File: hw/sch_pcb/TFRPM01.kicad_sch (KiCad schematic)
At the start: 28 parts, among them J1 DS1022-1*40RDF11-B, J2 SM04B-GHS-TB, J3 SM04B-GHS-TB, M2 M3, U1 PCF8583T, U2 SN74LVC1G14QDCKRQ1, U3 MIC5504-3.3YM5

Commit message: Cleanup schematics.
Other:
- moved on the sheet: J3, R10

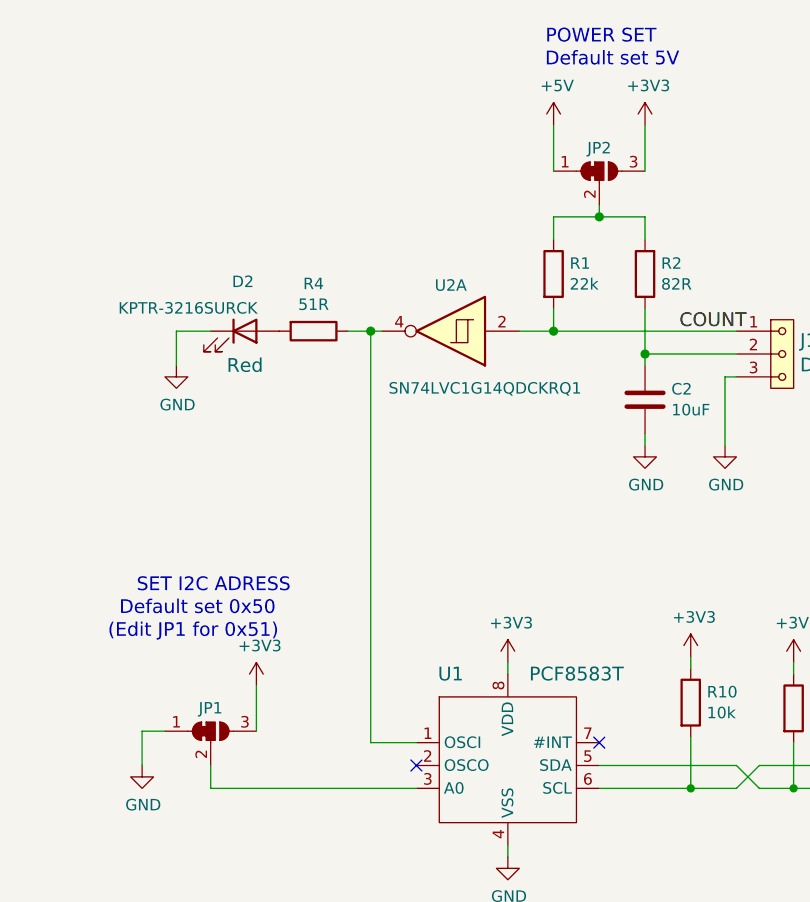
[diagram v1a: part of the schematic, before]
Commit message: Update schematics symbols and PCBs to resolve errors in action run.
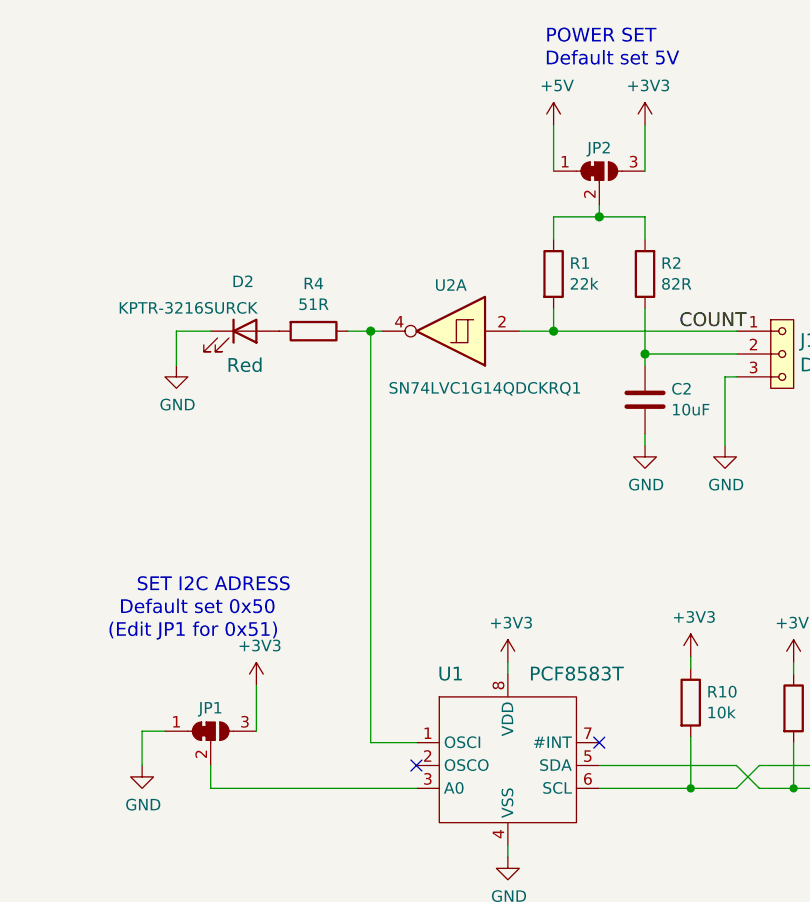
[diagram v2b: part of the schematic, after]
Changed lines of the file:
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@@
       (effects (font (size 1.524 1.524)) hide)
     )
-    (property "Datasheet" "" (at 35.56 175.26 0)
+    (property "Datasheet" "~" (at 35.56 175.26 0)
       (effects (font (size 1.524 1.524)))
     )
@@
       (effects (font (size 1.524 1.524)) hide)
     )
-    (property "Datasheet" "" (at 133.35 95.25 0)
+    (property "Datasheet" "https://www.nxp.com/docs/en/data-sheet/PCF8583.pdf" (at 133.35 95.25 0)
       (effects (font (size 1.524 1.524)) hide)
     )
@@
       (effects (font (size 1.27 1.27)) hide)
     )
-    (property "Datasheet" "" (at 165.1 105.41 0)
+    (property "Datasheet" "~" (at 165.1 105.41 0)
       (effects (font (size 1.27 1.27)) hide)
     )
@@
       (effects (font (size 1.27 1.27)) hide)
     )
-    (property "Datasheet" "" (at 153.67 104.775 0)
+    (property "Datasheet" "~" (at 153.67 104.775 0)
       (effects (font (size 1.27 1.27)) hide)
     )
@@
       (effects (font (size 1.524 1.524)) hide)
     )
-    (property "Datasheet" "" (at 27.94 175.26 0)
+    (property "Datasheet" "~" (at 27.94 175.26 0)
       (effects (font (size 1.524 1.524)))
     )
@@
     )
     (property "Datasheet" "http://www.ti.com/lit/gpn/sn74HC14" (at 127 63.5 0)
-      (effects (font (size 1.27 1.27)) hide)
-    )
-    (property "UST_id" "" (at 127 63.5 0)
       (effects (font (size 1.27 1.27)) hide)
     )
@@
     )
   )
-  (symbol (lib_name "LED_1") (lib_id "Device:LED") (at 104.14 63.5 0) (unit 1)
+  (symbol (lib_id "Device:LED") (at 104.14 63.5 0) (unit 1)
     (in_bom yes) (on_board yes) (dnp no)
     (property "Reference" "D2" (at 103.9114 58.0136 0)
@@
       (effects (font (size 1.27 1.27)) hide)
     )
-    (property "Datasheet" "https://www.tme.eu/Document/abfabb2e369b55022af776cff528b52b/kptr-3216surck.pdf" (at 104.14 63.5 0)
+    (property "Datasheet" "~" (at 104.14 63.5 0)
       (effects (font (size 1.27 1.27)) hide)
     )
@@
       (effects (font (size 1.27 1.27)) hide)
     )
-    (property "Datasheet" "" (at 138.43 57.15 0)
+    (property "Datasheet" "~" (at 138.43 57.15 0)
       (effects (font (size 1.27 1.27)) hide)
     )
@@
       (effects (font (size 1.27 1.27)) hide)
     )
-    (property "Datasheet" "" (at 111.76 63.5 0)
+    (property "Datasheet" "~" (at 111.76 63.5 0)
       (effects (font (size 1.27 1.27)) hide)
     )
@@
       (effects (font (size 1.27 1.27)) hide)
     )
-    (property "Datasheet" "" (at 148.59 71.12 0)
+    (property "Datasheet" "~" (at 148.59 71.12 0)
       (effects (font (size 1.27 1.27)) hide)
     )
@@
     )
     (property "Datasheet" "http://ww1.microchip.com/downloads/en/DeviceDoc/MIC550X.pdf" (at 60.96 165.1 0)
-      (effects (font (size 1.27 1.27)) hide)
-    )
-    (property "UST_id" "" (at 67.31 171.45 0)
       (effects (font (size 1.27 1.27)) hide)
     )
@@
       (effects (font (size 1.524 1.524)) hide)
     )
-    (property "Datasheet" "" (at 26.67 137.16 0)
+    (property "Datasheet" "~" (at 26.67 137.16 0)
       (effects (font (size 1.524 1.524)))
     )
@@
       (effects (font (size 1.524 1.524)) hide)
     )
-    (property "Datasheet" "" (at 35.56 137.16 0)
+    (property "Datasheet" "~" (at 35.56 137.16 0)
       (effects (font (size 1.524 1.524)))
     )
@@
       (effects (font (size 1.27 1.27)) hide)
     )
-    (property "Datasheet" "" (at 81.28 175.26 0)
+    (property "Datasheet" "~" (at 81.28 175.26 0)
       (effects (font (size 1.27 1.27)) hide)
     )
@@
     )
     (property "Datasheet" "http://www.ti.com/lit/gpn/sn74HC14" (at 53.34 137.16 0)
-      (effects (font (size 1.27 1.27)) hide)
-    )
-    (property "UST_id" "" (at 53.34 137.16 0)
       (effects (font (size 1.27 1.27)) hide)
     )
@@
       (effects (font (size 1.27 1.27)) hide)
     )
-    (property "Datasheet" "" (at 148.59 57.15 0)
+    (property "Datasheet" "~" (at 148.59 57.15 0)
       (effects (font (size 1.27 1.27)) hide)
     )
@@
       (effects (font (size 1.27 1.27)) hide)
     )
-    (property "Datasheet" "" (at 72.39 143.51 0)
+    (property "Datasheet" "~" (at 72.39 143.51 0)
       (effects (font (size 1.27 1.27)) hide)
     )
@@
       (effects (font (size 1.27 1.27)) hide)
     )
-    (property "Datasheet" "https://www.tme.eu/Document/283cf8402cc8d70fa16840405395cb5a/kptr-3216cgck.pdf" (at 72.39 135.89 0)
+    (property "Datasheet" "~" (at 72.39 135.89 0)
       (effects (font (size 1.27 1.27)) hide)
     )
@@
     )
   )
-  (symbol (lib_name "SolderJumper_3_Bridged12_1") (lib_id "Jumper:SolderJumper_3_Bridged12") (at 143.51 45.72 0) (unit 1)
+  (symbol (lib_id "Jumper:SolderJumper_3_Bridged12") (at 143.51 45.72 0) (unit 1)
     (in_bom no) (on_board yes) (dnp no)
     (property "Reference" "JP2" (at 143.51 43.1608 0)
